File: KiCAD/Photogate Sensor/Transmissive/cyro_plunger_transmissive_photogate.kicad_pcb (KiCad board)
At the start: 2 copper layers, 122 x 70 mm, 45 parts, among them J2 FFC Socket, J3 USB_B_Micro, J4 UPDI socket, J6 Conn_01x03_Socket, Q1 Q_NMOS_GSD, Q2 Q_NMOS_GSD, Q3 Q_NMOS_GSD, Q4 Q_NMOS_GSD, U1 5V LDO, U2 Opamp_Dual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

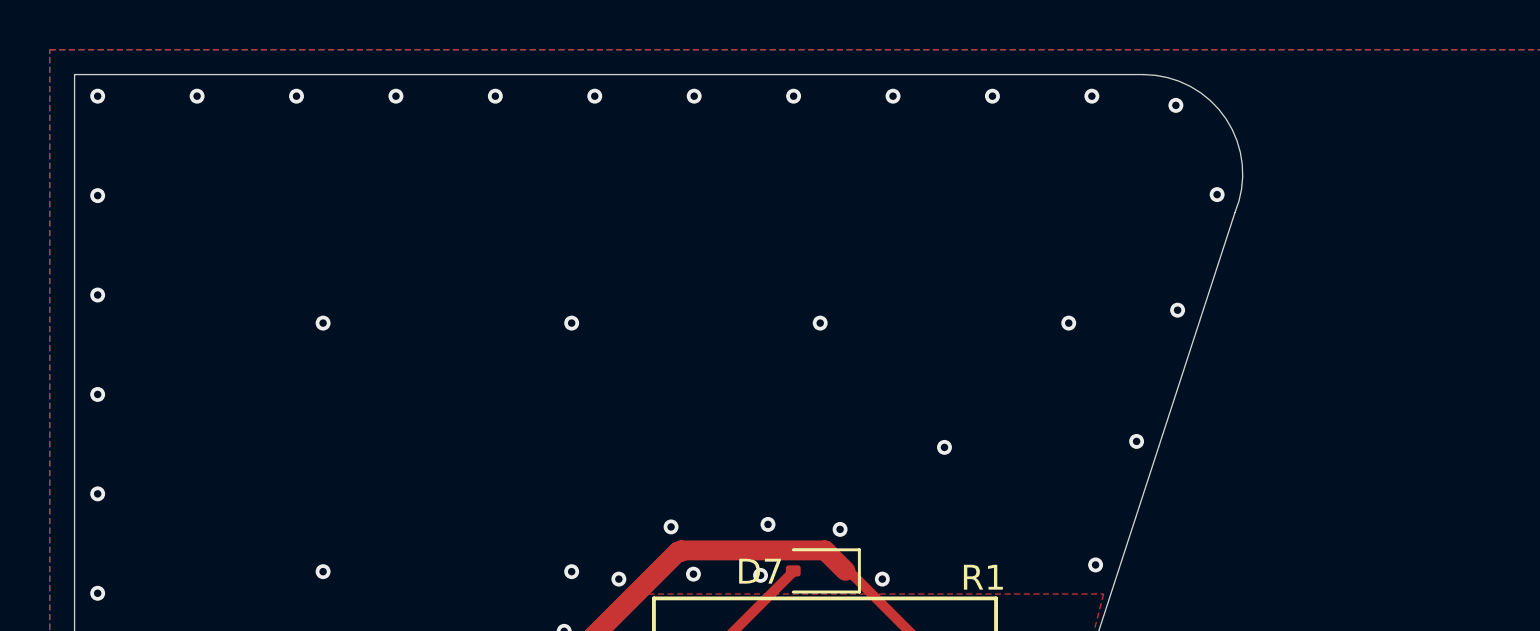
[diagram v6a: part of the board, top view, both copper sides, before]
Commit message: A license info to board
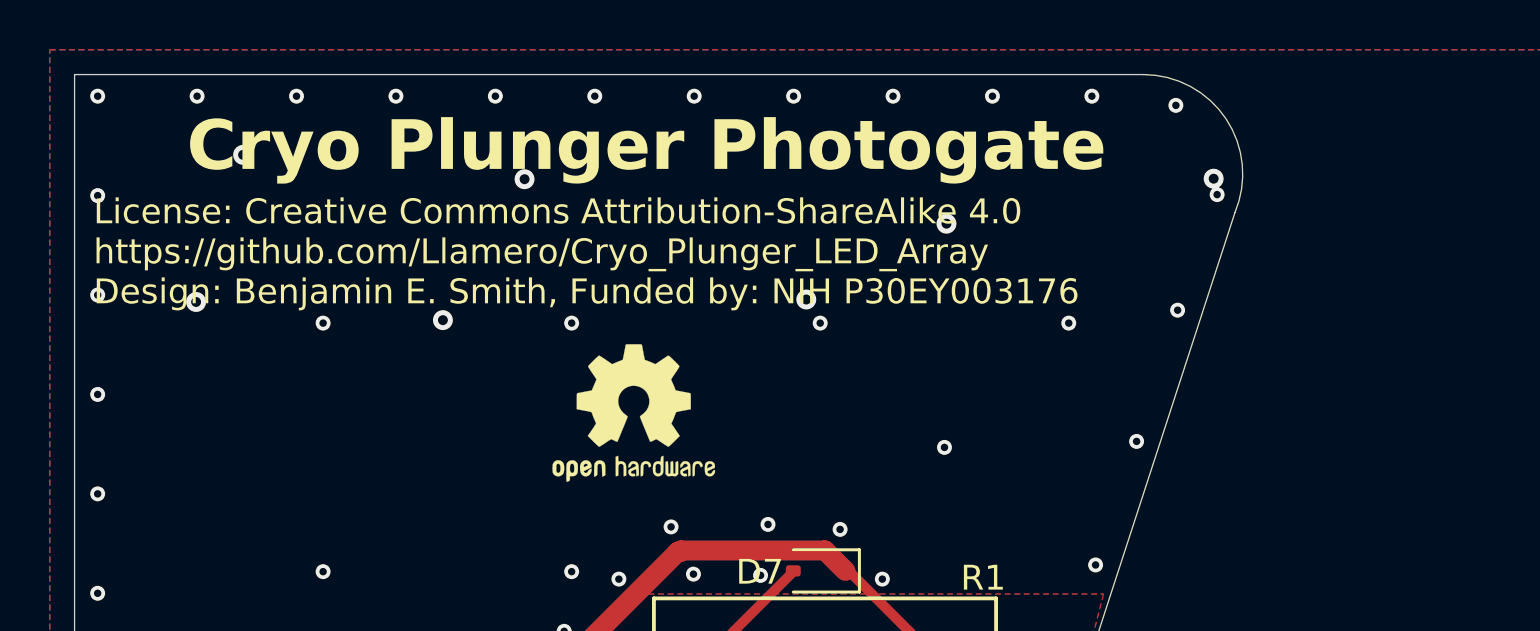
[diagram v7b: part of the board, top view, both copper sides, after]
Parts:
- added SYM3: Logo_Open_Hardware_Small, Symbol:OSHW-Logo2_7.3x6mm_SilkScreen, F.Cu at (122.5, 113.6)
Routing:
- net GND: vias 571 -> 578
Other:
- board text added: "Cryo Plunger Photogate"
- board text added: "License: Creative Commons Attribution-ShareAlike 4.0 https://github.com/Llamero/Cryo_Plunger_LED_Array Design: Benjamin E. Smith, Funded by: NIH P30EY003176"
